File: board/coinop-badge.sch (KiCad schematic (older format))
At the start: 36 parts, among them CON1 AVR-ISP-6, J1 Conn_01x02, SW1 SW_Push, SW2 SW_Push, U1 ATMEGA48A-AU

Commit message: Removed erroneous connection left over from larger charlieplex array
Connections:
- net CHARLIE-4: no longer names the net of U1.30 ((PCINT16/RXD)PD0)
- net CHARLIE-4: no longer RN2.2 (R2.1)
- no-connect marks 2 -> 5
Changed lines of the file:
@@
 Text GLabel 6100 1650 0    60   Input ~ 0
 CHARLIE-2
-Text GLabel 6100 3700 0    60   Input ~ 0
-CHARLIE-4
 Text GLabel 7050 1300 1    60   Input ~ 0
 ENG-1
@@
 Text GLabel 4750 3950 2    60   Input ~ 0
 CHARLIE-3
-Text GLabel 4150 3850 2    60   Input ~ 0
-CHARLIE-4
 Text GLabel 4150 4050 2    60   Input ~ 0
 SHIELD-1
@@
 	6950 2050 7050 2050
 Wire Wire Line
-	6450 4200 6600 4200
-Wire Wire Line
-	6450 3700 6450 4200
-Wire Wire Line
-	6100 3700 6450 3700
-Wire Wire Line
 	6500 2050 6550 2050
 Wire Wire Line
@@
 Wire Wire Line
 	10000 4150 9900 4150
+NoConn ~ 4150 3850
+NoConn ~ 6600 4200
+NoConn ~ 7000 4200
 $EndSCHEMATC

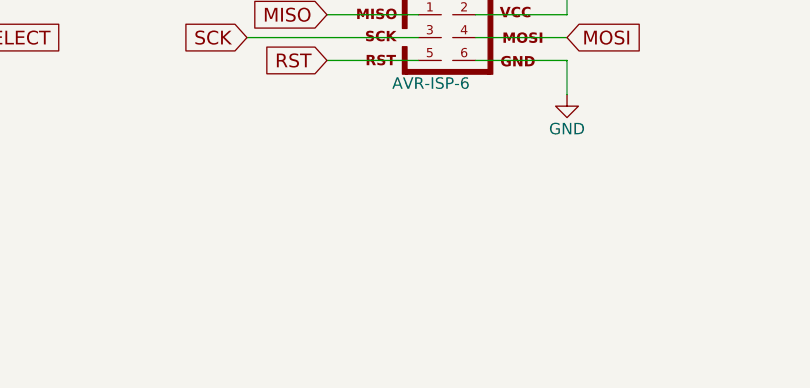
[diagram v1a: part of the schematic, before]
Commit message: Fixed button routing error Added SAO header (wired as add-on, not host) Added button labels
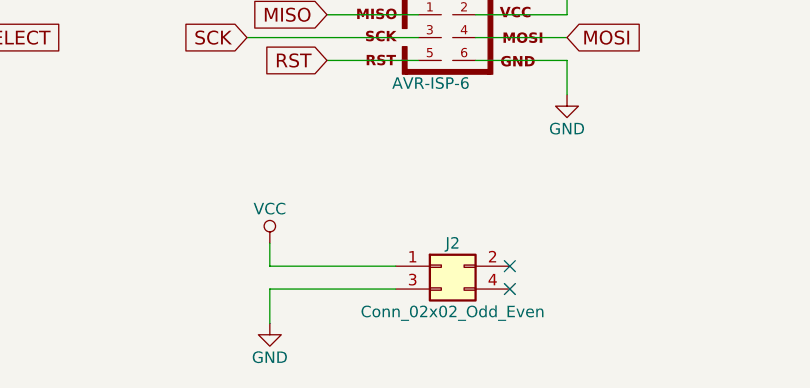
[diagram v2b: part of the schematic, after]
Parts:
- added J2: Conn_02x02_Odd_Even, Szczys:SAO_Pin_Header_Straight_2x02_Pitch2.54mm_SMD, symbol Conn_02x02_Odd_Even
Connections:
- net GND: now also J2.3 (Pin_3)
- net VCC: now also J2.1 (Pin_1)
- no-connect marks 5 -> 7
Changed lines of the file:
@@
 Title "Coin-Op Badge"
 Date ""
-Rev "1.0"
+Rev "2.1"
 Comp "Mike Szczys - Jumptuck.com"
 Comment1 ""
@@
 NoConn ~ 6600 4200
 NoConn ~ 7000 4200
+$Comp
+L VCC #PWR021
+U 1 1 5B484985
+P 4400 6800
+F 0 "#PWR021" H 4400 6650 50  0001 C CNN
+F 1 "VCC" H 4400 6950 50  0000 C CNN
+F 2 "" H 4400 6800 50  0001 C CNN
+F 3 "" H 4400 6800 50  0001 C CNN
+	1    4400 6800
+	1    0    0    -1
+$EndComp
+$Comp
+L GND #PWR022
+U 1 1 5B4849FF
+P 4400 7150
+F 0 "#PWR022" H 4400 6900 50  0001 C CNN
+F 1 "GND" H 4400 7000 50  0000 C CNN
+F 2 "" H 4400 7150 50  0001 C CNN
+F 3 "" H 4400 7150 50  0001 C CNN
+	1    4400 7150
+	1    0    0    -1
+$EndComp
+Wire Wire Line
+	4950 6900 4400 6900
+Wire Wire Line
+	4400 6900 4400 6800
+Wire Wire Line
+	4950 7000 4400 7000
+Wire Wire Line
+	4400 7000 4400 7150
+NoConn ~ 5450 6900
+NoConn ~ 5450 7000
+$Comp
+L Conn_02x02_Odd_Even J2
+U 1 1 5B486069
+P 5150 6900
+F 0 "J2" H 5200 7000 50  0000 C CNN
+F 1 "Conn_02x02_Odd_Even" H 5200 6700 50  0000 C CNN
+F 2 "Szczys:SAO_Pin_Header_Straight_2x02_Pitch2.54mm_SMD" H 5150 6900 50  0001 C CNN
+F 3 "" H 5150 6900 50  0001 C CNN
+	1    5150 6900
+	1    0    0    -1
+$EndComp
 $EndSCHEMATC
